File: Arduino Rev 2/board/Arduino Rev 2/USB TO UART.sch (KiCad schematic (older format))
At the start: 13 parts

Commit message: finished Schematic
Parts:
- removed J?: USB_B_Micro, symbol Connector:USB_B_Micro
- removed U?: FT230XS-R, digikey-footprints:SOIC-16_W3.90mm, symbol dk_Interface-Controllers:FT230XS-R
- added J401: 10103594-0001LF, Arduino Rev 2:USB_Micro_B_Female_10103594-0001LF, symbol arduino_symbols:10103594-0001LF
- added U401: FT231XS-U, Arduino Rev 2:SSOP-20_W3.9mm, symbol arduino_symbols:FT231XS-U
- C401, C402, C403, C404, C405, e401: renamed from C?; footprint (none) -> Arduino Rev 2:C_0603_1608Metric_Pad1.05x0.95mm_HandSolder
- D401: renamed from D?; footprint (none) -> Arduino Rev 2:led; symbol Device:LED -> arduino_symbols:LED
- FB401: renamed from FB?; footprint (none) -> Arduino Rev 2:R_0603_1608Metric_Pad1.05x0.95mm_HandSolder; symbol Device:Ferrite_Bead_Small -> arduino_symbols:Ferrite_Bead_Small; Digikey (none) -> 742792651
- R401, R402, R403: renamed from R?; footprint (none) -> Arduino Rev 2:R_0603_1608Metric_Pad1.05x0.95mm_HandSolder; symbol Device:R_US -> arduino_symbols:R_US
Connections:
- net labels added: DTR
- wire segments 41 -> 44
- no-connect marks 7 -> 10
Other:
- moved on the sheet: C401, C402, C403, C404, C405, D401, FB401, R401, R402, R403, e401

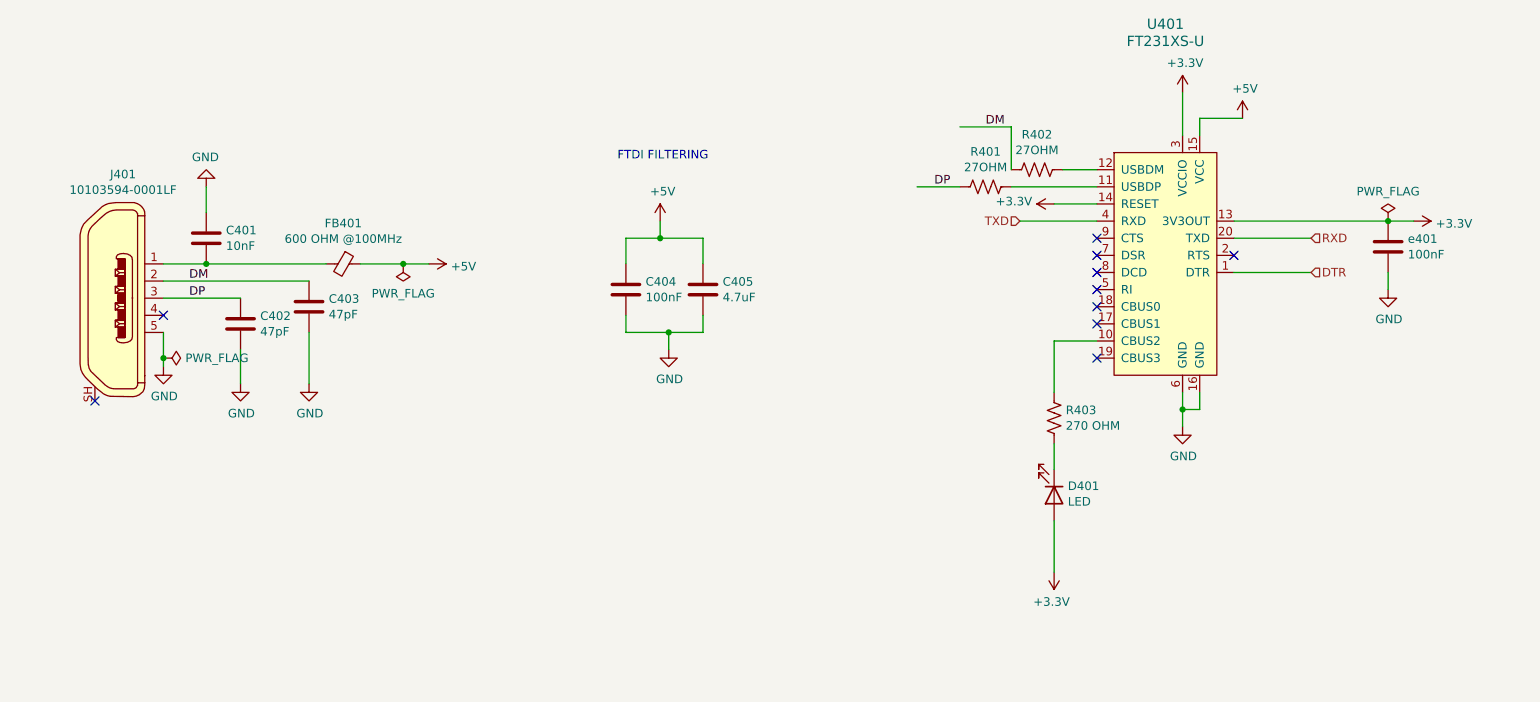
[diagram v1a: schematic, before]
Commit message: Fixed Schematic. Routing Finished
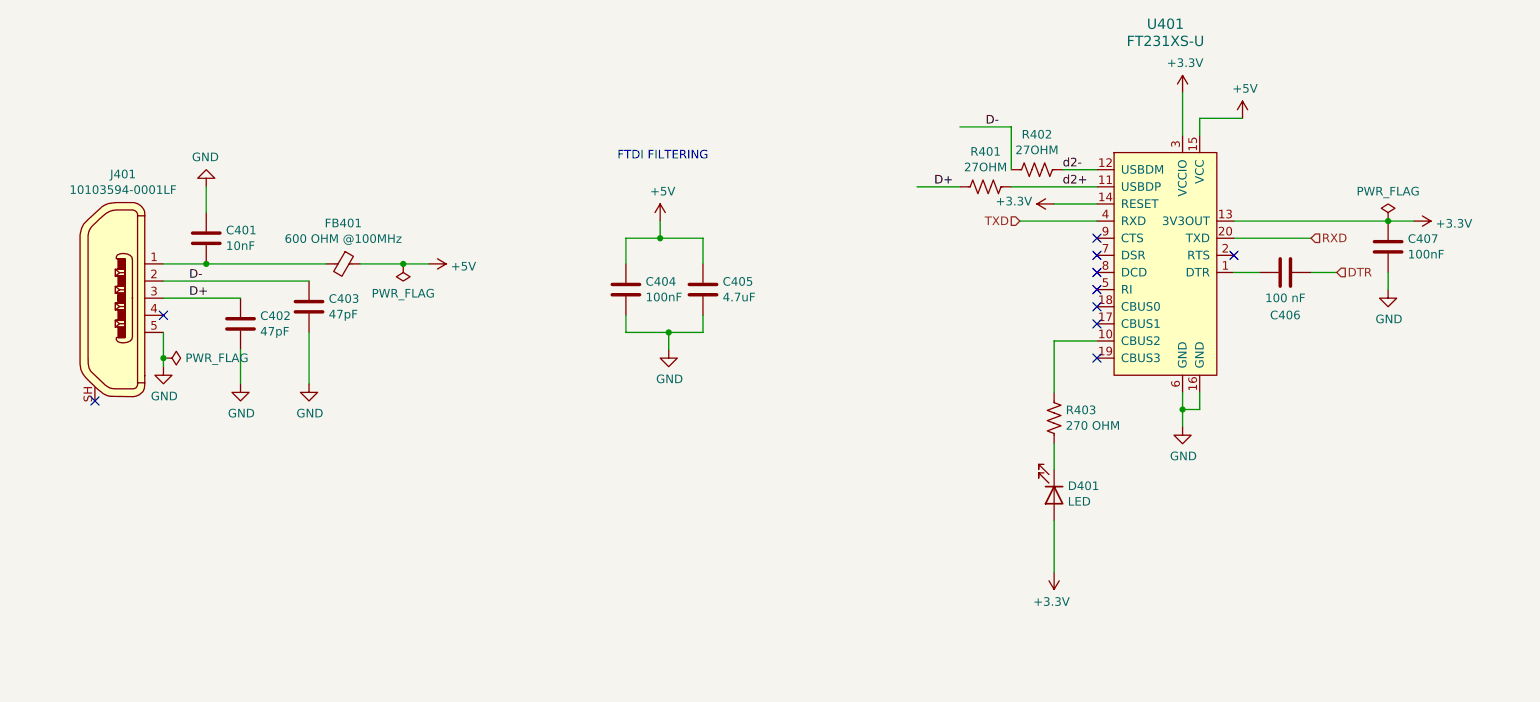
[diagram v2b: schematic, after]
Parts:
- added C406: 100 nF, Arduino Rev 2:C_0603_1608Metric_Pad1.05x0.95mm_HandSolder, symbol arduino_symbols:C
- renumbered e401 to C407
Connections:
- net labels added: D+, D-, d2+, d2-
- net labels removed: DM, DP
- wire segments 44 -> 45
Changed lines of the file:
@@
 $Descr A4 11693 8268
 encoding utf-8
-Sheet 4 6
+Sheet 3 6
 Title ""
 Date ""
@@
 	2550 3650 3000 3650
 Text Label 2700 3650 0    50   ~ 0
-DP
+D+
 Text Label 2700 3550 0    50   ~ 0
-DM
+D-
 Text Label 7350 2650 0    50   ~ 0
-DM
+D-
 Text Label 7050 3000 0    50   ~ 0
-DP
+D+
 $Comp
 L arduino_symbols:C C401
@@
 	6950 3000 7200 3000
 $Comp
-L arduino_symbols:C e401
+L arduino_symbols:C C407
 U 1 1 5F0F035F
 P 9700 3350
-F 0 "e401" H 9815 3396 50  0000 L CNN
+F 0 "C407" H 9815 3396 50  0000 L CNN
 F 1 "100nF" H 9815 3305 50  0000 L CNN
 F 2 "Arduino Rev 2:C_0603_1608Metric_Pad1.05x0.95mm_HandSolder" H 9738 3200 50  0001 C CNN
@@
 Wire Wire Line
 	8800 3200 9700 3200
-Text HLabel 9250 3500 2    50   Input ~ 0
+Text HLabel 9400 3500 2    50   Input ~ 0
 DTR
-Wire Wire Line
-	8800 3500 9250 3500
 Wire Wire Line
 	7750 3900 8000 3900
@@
 NoConn ~ 8800 3400
 $Comp
-L power:PWR_FLAG #FLG0401
+L power:PWR_FLAG #FLG0402
 U 1 1 5F0E1839
 P 3950 3450
-F 0 "#FLG0401" H 3950 3525 50  0001 C CNN
+F 0 "#FLG0402" H 3950 3525 50  0001 C CNN
 F 1 "PWR_FLAG" H 3950 3623 50  0000 C CNN
 F 2 "" H 3950 3450 50  0001 C CNN
@@
 	3950 3450 3700 3450
 $Comp
-L power:PWR_FLAG #FLG0402
+L power:PWR_FLAG #FLG0403
 U 1 1 5F0E1D22
 P 9700 3200
-F 0 "#FLG0402" H 9700 3275 50  0001 C CNN
+F 0 "#FLG0403" H 9700 3275 50  0001 C CNN
 F 1 "PWR_FLAG" H 9700 3373 50  0000 C CNN
 F 2 "" H 9700 3200 50  0001 C CNN
@@
 NoConn ~ 2150 4250
 $Comp
-L power:PWR_FLAG #FLG0101
+L power:PWR_FLAG #FLG0401
 U 1 1 5F0F6831
 P 2550 4000
-F 0 "#FLG0101" H 2550 4075 50  0001 C CNN
+F 0 "#FLG0401" H 2550 4075 50  0001 C CNN
 F 1 "PWR_FLAG" V 2550 4128 50  0000 L CNN
 F 2 "" H 2550 4000 50  0001 C CNN
@@
 Wire Wire Line
 	2550 4000 2550 4050
+Text Label 7800 3000 0    50   ~ 0
+d2+
+Text Label 7800 2900 0    50   ~ 0
+d2-
+$Comp
+L arduino_symbols:C C406
+U 1 1 5F118027
+P 9100 3500
+F 0 "C406" V 9350 3500 50  0000 C CNN
+F 1 "100 nF" V 9250 3500 50  0000 C CNN
+F 2 "Arduino Rev 2:C_0603_1608Metric_Pad1.05x0.95mm_HandSolder" H 9138 3350 50  0001 C CNN
+F 3 "~" H 9100 3500 50  0001 C CNN
+	1    9100 3500
+	0    1    1    0
+$EndComp
+Wire Wire Line
+	8800 3500 8950 3500
+Wire Wire Line
+	9250 3500 9400 3500
 $EndSCHEMATC

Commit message: Final Board Design
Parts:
- C401: Digikey (none) -> C0603C103J5RACTU
- C402, C403: Digikey (none) -> CC0603JRNPO9BN470
- C404, C406, C407: Digikey (none) -> CC0603JRX7R7BB104
- C405: Digikey (none) -> CL10A475MQ5LNNC
- D401: Digikey (none) -> LTST-C171KGKT
- FB401: Digikey 742792651 -> MPZ1608S601ATA00
- R401, R402: Digikey (none) -> RC0603FR-0727RL
- R403: Digikey (none) -> CRGP0603F270R
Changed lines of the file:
@@
 F 2 "Arduino Rev 2:C_0603_1608Metric_Pad1.05x0.95mm_HandSolder" H 2838 3150 50  0001 C CNN
 F 3 "~" H 2800 3300 50  0001 C CNN
+F 4 "C0603C103J5RACTU" H 2800 3300 50  0001 C CNN "Digikey"
 	1    2800 3300
 	1    0    0    -1
@@
 F 2 "Arduino Rev 2:C_0603_1608Metric_Pad1.05x0.95mm_HandSolder" H 3038 3650 50  0001 C CNN
 F 3 "~" H 3000 3800 50  0001 C CNN
+F 4 "CC0603JRNPO9BN470" H 3000 3800 50  0001 C CNN "Digikey"
 	1    3000 3800
 	1    0    0    -1
@@
 F 2 "Arduino Rev 2:C_0603_1608Metric_Pad1.05x0.95mm_HandSolder" H 3438 3550 50  0001 C CNN
 F 3 "~" H 3400 3700 50  0001 C CNN
+F 4 "CC0603JRNPO9BN470" H 3400 3700 50  0001 C CNN "Digikey"
 	1    3400 3700
 	1    0    0    -1
@@
 F 2 "Arduino Rev 2:C_0603_1608Metric_Pad1.05x0.95mm_HandSolder" H 5288 3450 50  0001 C CNN
 F 3 "~" H 5250 3600 50  0001 C CNN
+F 4 "CC0603JRX7R7BB104" H 5250 3600 50  0001 C CNN "Digikey"
 	1    5250 3600
 	1    0    0    -1
@@
 F 2 "Arduino Rev 2:C_0603_1608Metric_Pad1.05x0.95mm_HandSolder" H 5738 3450 50  0001 C CNN
 F 3 "~" H 5700 3600 50  0001 C CNN
+F 4 "CL10A475MQ5LNNC" H 5700 3600 50  0001 C CNN "Digikey"
 	1    5700 3600
 	1    0    0    -1
@@
 F 2 "Arduino Rev 2:R_0603_1608Metric_Pad1.05x0.95mm_HandSolder" V 3530 3450 50  0001 C CNN
 F 3 "~" H 3600 3450 50  0001 C CNN
-F 4 "742792651" V 3600 3450 50  0001 C CNN "Digikey"
+F 4 "MPZ1608S601ATA00" V 3600 3450 50  0001 C CNN "Digikey"
 	1    3600 3450
 	0    1    1    0
@@
 F 2 "Arduino Rev 2:R_0603_1608Metric_Pad1.05x0.95mm_HandSolder" V 7690 2890 50  0001 C CNN
 F 3 "~" H 7650 2900 50  0001 C CNN
+F 4 "RC0603FR-0727RL" V 7650 2900 50  0001 C CNN "Digikey"
 	1    7650 2900
 	0    1    1    0
@@
 F 2 "Arduino Rev 2:R_0603_1608Metric_Pad1.05x0.95mm_HandSolder" V 7390 2990 50  0001 C CNN
 F 3 "~" H 7350 3000 50  0001 C CNN
+F 4 "RC0603FR-0727RL" V 7350 3000 50  0001 C CNN "Digikey"
 	1    7350 3000
 	0    1    1    0
@@
 F 2 "Arduino Rev 2:C_0603_1608Metric_Pad1.05x0.95mm_HandSolder" H 9738 3200 50  0001 C CNN
 F 3 "~" H 9700 3350 50  0001 C CNN
+F 4 "CC0603JRX7R7BB104" H 9700 3350 50  0001 C CNN "Digikey"
 	1    9700 3350
 	1    0    0    -1
@@
 F 2 "Arduino Rev 2:led" H 7750 4800 50  0001 C CNN
 F 3 "~" H 7750 4800 50  0001 C CNN
+F 4 "LTST-C171KGKT" V 7750 4800 50  0001 C CNN "Digikey"
 	1    7750 4800
 	0    1    1    0
@@
 F 2 "Arduino Rev 2:R_0603_1608Metric_Pad1.05x0.95mm_HandSolder" V 7790 4340 50  0001 C CNN
 F 3 "~" H 7750 4350 50  0001 C CNN
+F 4 "CRGP0603F270R" H 7750 4350 50  0001 C CNN "Digikey"
 	1    7750 4350
 	-1   0    0    1
@@
 F 2 "Arduino Rev 2:C_0603_1608Metric_Pad1.05x0.95mm_HandSolder" H 9138 3350 50  0001 C CNN
 F 3 "~" H 9100 3500 50  0001 C CNN
+F 4 "CC0603JRX7R7BB104" V 9100 3500 50  0001 C CNN "Digikey"
 	1    9100 3500
 	0    1    1    0
